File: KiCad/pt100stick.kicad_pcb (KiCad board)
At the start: 2 copper layers, 15.7 x 20.8 mm, 10 parts, among them U1 MAX31865ATP_

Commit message: Slight tweaks
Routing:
- net /RTDIN-: track 16.1 -> 16.8 mm
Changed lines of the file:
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@@
     (thickness 1.6)
     (drawings 32)
-    (tracks 110)
+    (tracks 109)
     (zones 0)
     (modules 10)
@@
   )
   (setup
-    (last_trace_width 0.25)
+    (last_trace_width 0.3)
     (user_trace_width 0.3)
     (user_trace_width 0.4)
@@
     (add_net /SCK)
     (add_net GND)
-    (add_net "Net-(A1-Pad1)")
-    (add_net "Net-(A1-Pad15)")
-    (add_net "Net-(A1-Pad16)")
-    (add_net "Net-(A1-Pad8)")
-    (add_net "Net-(A1-Pad9)")
     (add_net "Net-(R1-Pad1)")
-    (add_net "Net-(U1-Pad17)")
-    (add_net "Net-(U1-Pad18)")
     (add_net VDDA)
   )
@@
   (segment (start 152.4765 83.8965) (end 154.94 86.36) (width 0.25) (layer F.Cu) (net 2) (status 20))
   (segment (start 152.4765 74.833) (end 152.4765 83.8965) (width 0.25) (layer F.Cu) (net 2) (status 10))
+  (segment (start 153.73902 74.040022) (end 153.73902 80.07902) (width 0.25) (layer F.Cu) (net 3))
+  (segment (start 153.231998 73.533) (end 153.73902 74.040022) (width 0.25) (layer F.Cu) (net 3))
   (segment (start 153.73902 80.07902) (end 154.94 81.28) (width 0.25) (layer F.Cu) (net 3) (status 20))
-  (segment (start 153.1254 73.70799) (end 153.73902 74.32161) (width 0.25) (layer F.Cu) (net 3))
-  (segment (start 152.4765 73.533) (end 152.65149 73.70799) (width 0.25) (layer F.Cu) (net 3) (status 10))
-  (segment (start 153.73902 74.32161) (end 153.73902 80.07902) (width 0.25) (layer F.Cu) (net 3))
-  (segment (start 152.65149 73.70799) (end 153.1254 73.70799) (width 0.25) (layer F.Cu) (net 3))
+  (segment (start 152.4765 73.533) (end 153.231998 73.533) (width 0.25) (layer F.Cu) (net 3) (status 10))
   (segment (start 153.28901 74.50801) (end 153.28901 82.16901) (width 0.25) (layer F.Cu) (net 4))
   (segment (start 152.4765 74.183) (end 152.964 74.183) (width 0.25) (layer F.Cu) (net 4) (status 10))
@@
   (segment (start 144.159 71.12) (end 144.159 70.645) (width 0.25) (layer F.Cu) (net 6) (status 30))
   (segment (start 144.173 71.32349) (end 144.173 71.12) (width 0.25) (layer F.Cu) (net 6) (status 30))
-  (segment (start 143.1798 73.66) (end 144.1958 72.644) (width 0.3) (layer F.Cu) (net 6))
-  (segment (start 142.24 73.66) (end 143.1798 73.66) (width 0.3) (layer F.Cu) (net 6))
-  (segment (start 144.1958 71.1428) (end 144.173 71.12) (width 0.3) (layer F.Cu) (net 6))
-  (segment (start 144.1958 72.644) (end 144.1958 71.1428) (width 0.3) (layer F.Cu) (net 6))
+  (segment (start 143.1798 73.66) (end 144.1958 72.644) (width 0.3) (layer F.Cu) (net 6) (status 20))
+  (segment (start 142.24 73.66) (end 143.1798 73.66) (width 0.3) (layer F.Cu) (net 6) (status 10))
+  (segment (start 144.1958 71.1428) (end 144.173 71.12) (width 0.3) (layer F.Cu) (net 6) (status 30))
+  (segment (start 144.1958 72.644) (end 144.1958 71.1428) (width 0.3) (layer F.Cu) (net 6) (status 30))
   (segment (start 144.49651 76.073) (end 145.3255 75.24401) (width 0.25) (layer F.Cu) (net 7) (status 10))
   (segment (start 144.3 76.073) (end 144.49651 76.073) (width 0.25) (layer F.Cu) (net 7) (status 30))
@@
   (segment (start 146.939 75.582) (end 146.448 76.073) (width 0.25) (layer F.Cu) (net 8))
   (segment (start 146.939 74.592298) (end 146.939 75.582) (width 0.25) (layer F.Cu) (net 8))
-  (segment (start 143.786 77.746) (end 145.034 77.746) (width 0.5) (layer F.Cu) (net 9) (status 20))
-  (segment (start 142.24 76.2) (end 143.786 77.746) (width 0.5) (layer F.Cu) (net 9) (status 10))
-  (segment (start 147.7515 75.868788) (end 147.7515 74.833) (width 0.5) (layer F.Cu) (net 9) (status 20))
-  (segment (start 145.874288 77.746) (end 147.7515 75.868788) (width 0.5) (layer F.Cu) (net 9))
-  (segment (start 145.034 77.746) (end 145.874288 77.746) (width 0.5) (layer F.Cu) (net 9) (status 10))
+  (segment (start 147.7515 75.776092) (end 147.7515 74.833) (width 0.3) (layer F.Cu) (net 9) (status 20))
+  (segment (start 145.781592 77.746) (end 147.7515 75.776092) (width 0.3) (layer F.Cu) (net 9) (status 10))
+  (segment (start 145.034 77.746) (end 145.781592 77.746) (width 0.3) (layer F.Cu) (net 9) (status 30))
+  (segment (start 143.786 77.746) (end 142.24 76.2) (width 0.3) (layer F.Cu) (net 9))
+  (segment (start 145.034 77.746) (end 143.786 77.746) (width 0.3) (layer F.Cu) (net 9))
   (segment (start 142.606 83.454) (end 142.24 83.82) (width 0.25) (layer F.Cu) (net 10) (status 30))
   (segment (start 143.525 85.105) (end 142.24 83.82) (width 0.3) (layer F.Cu) (net 10) (status 20))
@@
   (segment (start 145.034 83.805) (end 147.416692 83.805) (width 0.3) (layer F.Cu) (net 11) (status 10))
   (segment (start 145.034 82.282) (end 145.034 83.805) (width 0.3) (layer F.Cu) (net 11) (status 30))
-  (segment (start 144.032 81.28) (end 145.034 82.282) (width 0.3) (layer F.Cu) (net 11) (status 20))
-  (segment (start 142.24 81.28) (end 144.032 81.28) (width 0.3) (layer F.Cu) (net 11) (status 10))
+  (segment (start 144.765 83.805) (end 145.034 83.805) (width 0.3) (layer F.Cu) (net 11))
+  (segment (start 142.24 81.28) (end 144.765 83.805) (width 0.3) (layer F.Cu) (net 11))
   (segment (start 142.748 78.232) (end 142.24 78.74) (width 0.25) (layer F.Cu) (net 12) (status 30))
   (segment (start 147.066 82.707) (end 147.798 82.707) (width 0.3) (layer F.Cu) (net 12) (status 30))
@@
   (segment (start 145.509 80.532) (end 145.965999 80.988999) (width 0.3) (layer F.Cu) (net 12))
   (segment (start 145.034 80.532) (end 145.509 80.532) (width 0.3) (layer F.Cu) (net 12) (status 10))
-  (segment (start 148.814 75.8955) (end 148.814 76.043) (width 0.3) (layer F.Cu) (net 13) (status 30))
-  (segment (start 148.814 76.043) (end 148.844 76.073) (width 0.3) (layer F.Cu) (net 13) (status 30))
+  (segment (start 148.814 75.8955) (end 148.814 76.1538) (width 0.3) (layer F.Cu) (net 13) (status 30))
+  (segment (start 148.814 76.1538) (end 148.8186 76.1584) (width 0.3) (layer F.Cu) (net 13) (status 30))
   (segment (start 148.116 81.407) (end 147.066 81.407) (width 0.3) (layer F.Cu) (net 13) (status 20))
-  (segment (start 148.844 76.073) (end 148.844 80.679) (width 0.3) (layer F.Cu) (net 13) (status 10))
-  (segment (start 148.844 80.679) (end 148.116 81.407) (width 0.3) (layer F.Cu) (net 13))
+  (segment (start 148.8186 80.7044) (end 148.116 81.407) (width 0.3) (layer F.Cu) (net 13))
+  (segment (start 148.8186 76.1584) (end 148.8186 80.7044) (width 0.3) (layer F.Cu) (net 13) (status 10))
   (segment (start 148.741 71.12) (end 148.814 71.193) (width 0.25) (layer F.Cu) (net 14) (status 30))
   (segment (start 145.669 71.374) (end 145.923 71.12) (width 0.25) (layer F.Cu) (net 14) (status 30))

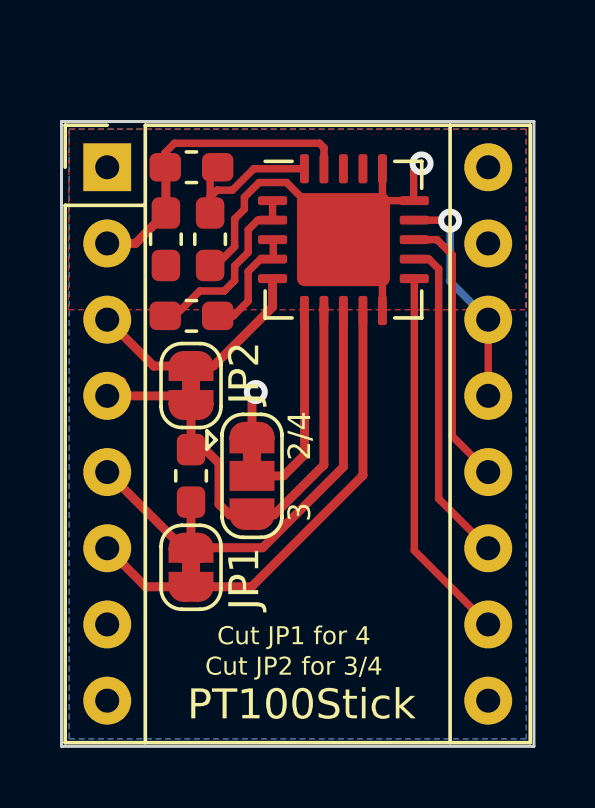
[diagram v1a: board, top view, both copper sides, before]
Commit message: enlarge holes
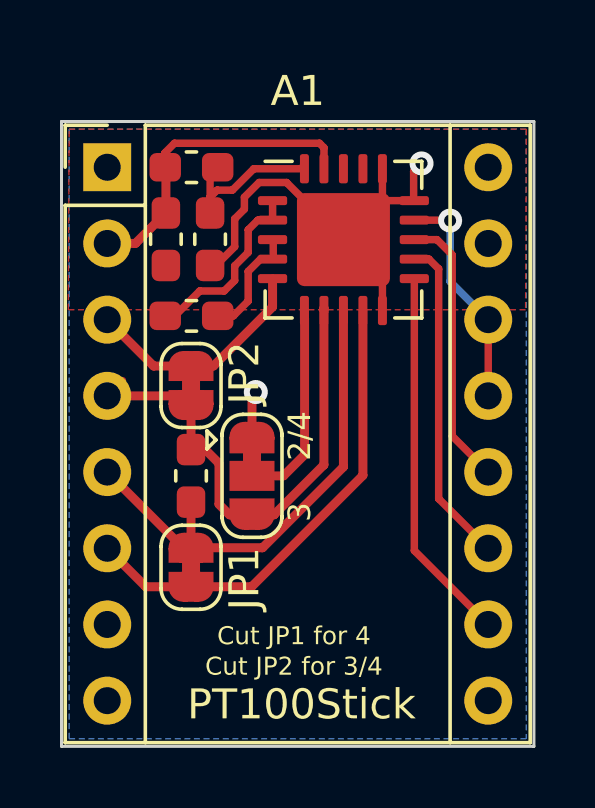
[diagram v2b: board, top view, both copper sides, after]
